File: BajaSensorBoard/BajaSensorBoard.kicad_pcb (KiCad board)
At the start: 2 copper layers, 50.8 x 25.4 mm, 18 parts, among them J1 ICSP, J2 POWER/CAN, J3 Conn_01x04, U1 ATtiny841-SS, U2 MCP25625-x-SS, U3 74HC04

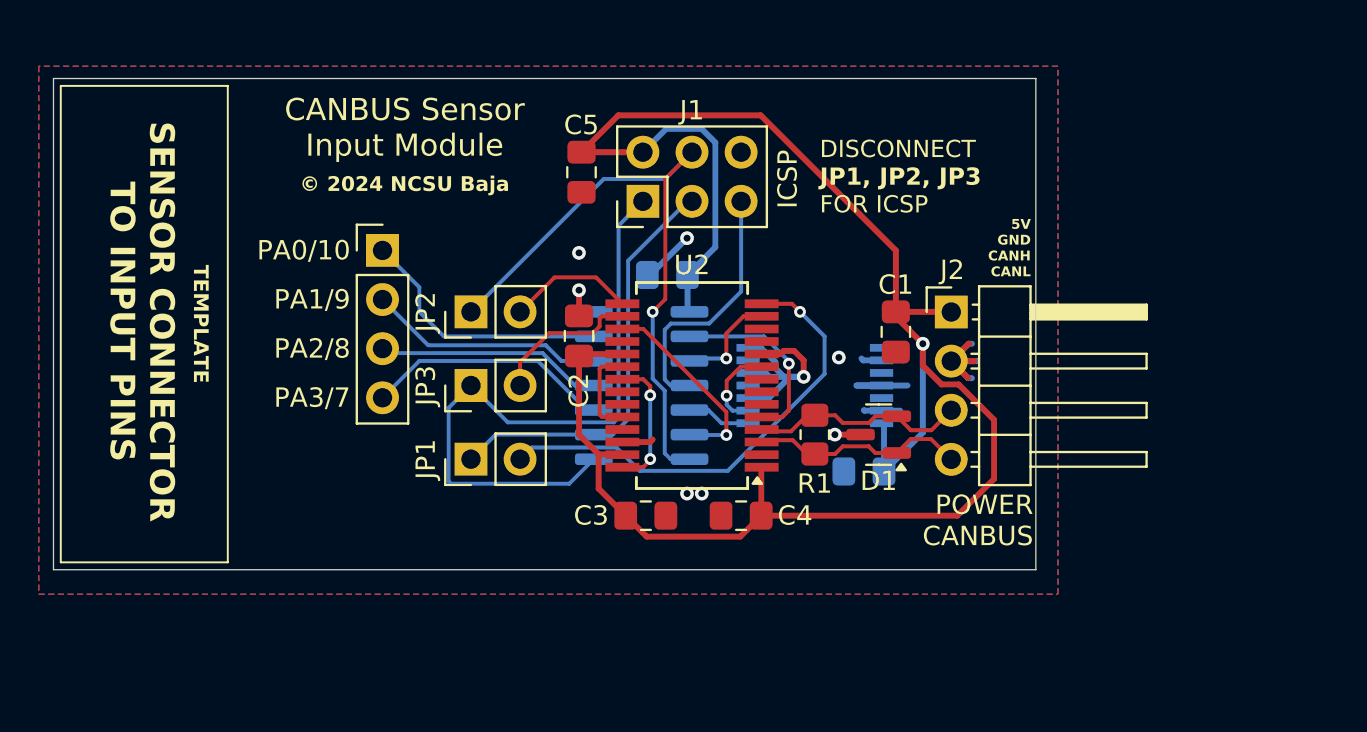
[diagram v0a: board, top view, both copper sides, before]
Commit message: Started new PCB layout (BajaSensorBoard)
Initial component layout and beginning traces (SPI and CAN first)
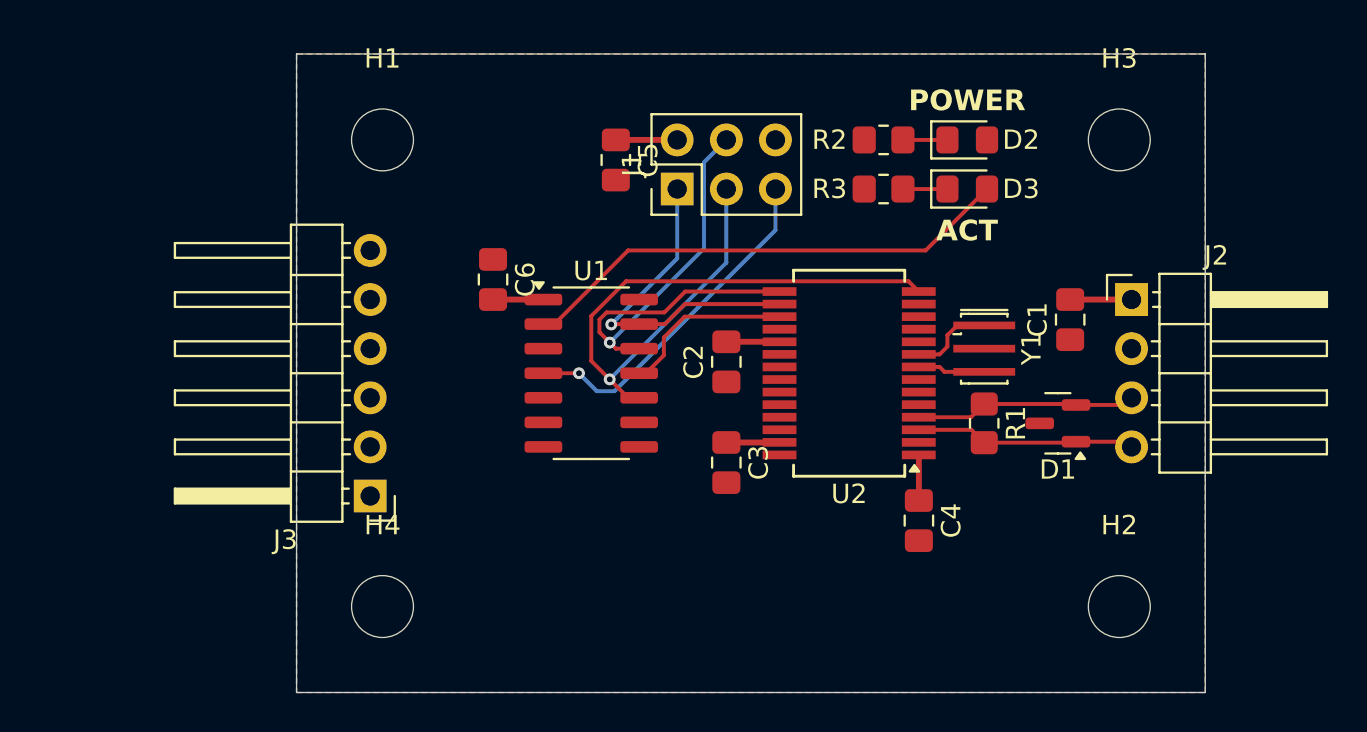
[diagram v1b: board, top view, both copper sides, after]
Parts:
- removed C7: 0.1u, Capacitor_SMD:C_0805_2012Metric_Pad1.18x1.45mm_HandSolder
- removed JP1, JP2, JP3: Jumper_2_Bridged, Connector_PinHeader_2.54mm:PinHeader_1x02_P2.54mm_Vertical
- removed U3: 74HC04, Package_SO:SSOP-14_5.3x6.2mm_P0.65mm
- added D2: POWER, LED_SMD:LED_0805_2012Metric_Pad1.15x1.40mm_HandSolder, F.Cu at (157.2, 92.1)
- added D3: ACT, LED_SMD:LED_0805_2012Metric_Pad1.15x1.40mm_HandSolder, F.Cu at (157.2, 94.6)
- added H1: MountingHole, MountingHole:MountingHole_3.2mm_M3, F.Cu at (127.0, 92.1)
- added H2: MountingHole, MountingHole:MountingHole_3.2mm_M3, F.Cu at (165.1, 116.2)
- added H3: MountingHole, MountingHole:MountingHole_3.2mm_M3, F.Cu at (165.1, 92.1)
- added H4: MountingHole, MountingHole:MountingHole_3.2mm_M3, F.Cu at (127.0, 116.2)
- added R2: 680, Resistor_SMD:R_0805_2012Metric_Pad1.20x1.40mm_HandSolder, F.Cu at (152.9, 92.1)
- added R3: 680, Resistor_SMD:R_0805_2012Metric_Pad1.20x1.40mm_HandSolder, F.Cu at (152.9, 94.6)
- added Y1: CSTNE16M0VH3C000R0, Crystal:Resonator_SMD_Murata_CSTxExxV-3Pin_3.0x1.1mm_HandSoldering, F.Cu at (158.1, 102.9)
- C6, U1: moved to F.Cu
- J3: value Conn_01x04 -> Conn_01x06; footprint Connector_PinHeader_2.54mm:PinHeader_1x04_P2.54mm_Vertical -> Connector_PinHeader_2.54mm:PinHeader_1x06_P2.54mm_Horizontal
- moved J3 12.7 mm to (126.4, 110.5), turned to 180 degrees
- moved J2 9.35 mm to (165.7, 100.3)
- moved D1 9.28 mm to (161.9, 106.7)
- moved C4 9.20 mm to (154.7, 111.8), turned to -90 degrees
- moved C1 9.04 mm to (162.6, 101.4)
- moved C6 9.02 mm to (132.7, 99.3), turned to -90 degrees
- moved R1 8.78 mm to (158.1, 106.7)
- moved U2 8.15 mm to (151.1, 104.1)
- moved C2 7.73 mm to (144.8, 103.6), turned to 90 degrees
- moved C3 4.99 mm to (144.8, 108.8), turned to -90 degrees
- moved U1 2.68 mm to (137.8, 104.1), turned to 0 degrees
- moved C5 1.89 mm to (139.1, 93.1)
- moved J1 1.89 mm to (142.2, 94.6)
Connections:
- J3 pad 1: /USER0 -> +5V
- J3 pad 2: /USER1 -> /USER0
- J3 pad 3: /USER2 -> /USER1
- J3 pad 4: /USER3 -> /USER2
- U1 pad 10: /USER3 -> /SCK
- U1 pad 11: /USER2 -> /~{SS}
- U1 pad 12: /USER1 -> /MOSI
- U1 pad 13: /USER0 -> /MISO
- U1 pad 2: /STBY -> /ACT
- U1 pad 5: /SYSCLK -> /USER3
- U1 pad 6: /~{SS} -> /USER2
- U1 pad 7: /MOSI -> /USER1
- U1 pad 8: /MISO -> /STBY
- U1 pad 9: /SCK -> /USER0
- U2 pad 14: Net-(JP1-B) -> /SCK
- U2 pad 15: Net-(JP2-B) -> /MOSI
- U2 pad 16: Net-(JP3-B) -> /MISO
- U2 pad 8: unconnected-(U2-OSC2-Pad8) -> Net-(U2-OSC2)
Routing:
- net +5V: track 100.3 -> 16.8 mm, vias 1 -> 0
- net GND: track 36.5 -> 0.00 mm, vias 8 -> 0
- net /ACT: track 0.00 -> 25.8 mm
- net Net-(JP1-B): track 24.5 -> 0.00 mm, vias 1 -> 0
- net /MISO: track 33.7 -> 17.6 mm, vias 0 -> 1
- net /SCK: track 21.8 -> 35.8 mm, vias 0 -> 1
- net /USER0: track 13.5 -> 0.00 mm
- net /USER3: track 12.8 -> 0.00 mm
- net /USER1: track 12.2 -> 0.00 mm
- net /USER2: track 11.7 -> 0.00 mm
- net /STBY: track 9.76 -> 0.00 mm, vias 1 -> 0
- net Net-(JP3-B): track 7.72 -> 0.00 mm
- net Net-(U2-RXD): track 7.00 -> 0.00 mm, vias 2 -> 0
- net /MOSI: track 32.9 -> 26.0 mm
- net Net-(JP2-B): track 6.59 -> 0.00 mm
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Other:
- board size 50.8 x 25.4 mm -> 47 x 33 mm
- board text removed: "5V GND CANH CANL"
- board text removed: "CANBUS Sensor Input Module"
- board text removed: "DISCONNECT FOR ICSP"
- board text removed: "ICSP"
- board text removed: "JP1, JP2, JP3"
- board text removed: "PA0/10"
- board text removed: "PA1/9"
- board text removed: "PA2/8"
- board text removed: "PA3/7"
- board text removed: "POWER CANBUS"
- board text removed: "SENSOR CONNECTOR TO INPUT PINS"
- board text removed: "TEMPLATE"
- board text removed: "© 2024 NCSU Baja"

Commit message: Finished routing (BajaSensorBoard)
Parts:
- moved Y1 0.64 mm to (158.8, 102.9)
- moved C2 0.42 mm to (145.0, 103.9)
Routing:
- net +5V: track 16.8 -> 116.0 mm, vias 0 -> 6
- net Net-(U1-XTAL2/PB1): track 0.00 -> 26.7 mm
- net /STBY: track 0.00 -> 16.2 mm, vias 0 -> 2
- net /USER0: track 0.00 -> 15.4 mm, vias 0 -> 2
- net /USER3: track 0.00 -> 11.1 mm
- net /USER2: track 0.00 -> 10.5 mm
- net /USER1: track 0.00 -> 10.0 mm
- net /MOSI: track 26.0 -> 16.8 mm
- net /SCK: track 35.8 -> 27.8 mm
- net /~{RESET}: track 18.0 -> 25.8 mm, vias 1 -> 0
- net Net-(U2-RXD): track 0.00 -> 7.64 mm, vias 0 -> 2
- net Net-(U2-TXD): track 0.00 -> 5.07 mm
- net GND: track 0.00 -> 3.62 mm, vias 0 -> 2
- net /MISO: track 17.6 -> 20.5 mm
- net Net-(U2-OSC2): track 3.49 -> 4.15 mm
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
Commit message: Final (?) PCB (BajaSensorBoard)
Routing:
- net /~{RESET}: track 25.8 -> 20.0 mm
- net GND: vias 2 -> 3
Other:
- board text added: "+"
- board text added: "-"
- board text added: "5V"
- board text added: "CAN Bus Input Module"
- board text added: "GND"
- board text added: "H"
- board text added: "L"
- board text added: "M3 Screws"
- board text added: "POWER CAN"
- board text added: "RXD"
- board text added: "SCL"
- board text added: "SDA"
- board text added: "TXD"
- board text added: "© 2025 NCSU Baja"

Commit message: Added logo
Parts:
- added G***: LOGO, obdbaja:baja_logo, B.Cu at (146.1, 104.1)
